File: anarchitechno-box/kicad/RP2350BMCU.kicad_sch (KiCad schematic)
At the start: 49 parts, among them J2 Conn_01x03_Socket, J4 C2988369, Q201 12mhz, SW1 C318884, U101 <value>, U201 TLV74311PDBVR, U21 C85364, U67 LP5907MFX-3.3

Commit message: Large intermediate schematic push. Remaining todos are on frontpage.
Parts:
- renumbered C3 to C10, C56 to C11, C28 to C12, C57 to C13, C58 to C14, C2 to C15, C4 to C16, C139 to C17, C5 to C18, C60 to C19, C26 to C20, C62 to C21, C33 to C22, C61 to C23, C150 to C24, C14 to C25, C16 to C26, C63 to C27, C65 to C28, C66 to C29, C51 to C3, C52 to C4, C53 to C5, C59 to C6, C54 to C7, C55 to C8, C140 to C9, J4 to J1, L3 to L1, Q201 to Q1, R204 to R1, R17 to R10, R18 to R11, R205 to R2, R33 to R3, R34 to R4, R35 to R5, R25 to R6, R202 to R7, R28 to R8, R26 to R9, U$2 to U$1, U101 to U4, U67 to U5, U201 to U6, U21 to U7, U3 to U8
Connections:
- net LED_STRING: now also U8.78 (GPIO1); no longer U8.79 (GPIO2)
- net PWM2_A: now reaches U8.1 (GPIO4)
- net PWM6_A: now reaches U8.11 (GPIO12)
- net PWM7_A: now reaches U8.13 (GPIO14)
- net ETH_MOSI: now reaches U8.19 (GPIO19)
- net ETH_MISO: now reaches U8.20 (GPIO20)
- net ETH_CS: now reaches U8.21 (GPIO21)
- net ETH_SCK: now reaches U8.22 (GPIO22)
- net DRV_SCK: now reaches U8.28 (GPIO27)
- net PWM3_A: now reaches U8.3 (GPIO6)
- net DRV_MOSI: now reaches U8.36 (GPIO28)
- net DRV_MISO: now reaches U8.38 (GPIO30)
- net DRV_nFAULT: now reaches U8.39 (GPIO31)
- net I2C0_SCL: now reaches U8.40 (GPIO32)
- net I2C0_SDA: now reaches U8.42 (GPIO33)
- net UART0_TX: now reaches U8.43 (GPIO34)
- net UART0_RX: now reaches U8.44 (GPIO35)
- net UART1_TX: now reaches U8.45 (GPIO36)
- net UART1_RX: now reaches U8.46 (GPIO37)
- net I2C1_SCL: now reaches U8.47 (GPIO38)
- net I2C1_SDA: now reaches U8.48 (GPIO39)
- net PWM8_A: now reaches U8.49 (GPIO40_ADC0)
- net DRV_CS1: now reaches U8.52 (GPIO41_ADC1)
- net PWM9_A: now reaches U8.53 (GPIO42_ADC2)
- net DRV_CS2: now reaches U8.54 (GPIO43_ADC3)
- net PWM10_A: now reaches U8.55 (GPIO44_ADC4)
- net DRV_CS3: now reaches U8.56 (GPIO45_ADC5)
- net PWM11_A: now reaches U8.57 (GPIO46_ADC6)
- net DRV_CS4: now reaches U8.58 (GPIO47_ADC7)
- net PWM4_A: now reaches U8.6 (GPIO8)
- net PWM0_A: now reaches U8.77 (GPIO0)
- net PWM5_A: now reaches U8.8 (GPIO10)
- new net PMW1_A: U8.79 (GPIO2)
- no-connect marks 35 -> 10
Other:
- moved on the sheet: C10, C11, C12, C13, C14, C15, C16, C17, C18, C19, C20, C21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

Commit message: meer Stijn in de Trein
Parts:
- added D16: SS34, Diode_SMD:D_SMA, symbol Diode:SS34
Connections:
- net +5V: now also D16.1 (K); no longer J1.A4B9 (VBUS), J1.A9B4 (VBUS)
- new net BREAKOUT_5V: D16.2 (A), J1.A4B9 (VBUS), J1.A9B4 (VBUS)
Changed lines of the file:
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@@
 	(wire
 		(pts
-			(xy 187.96 240.03) (xy 207.01 240.03)
+			(xy 187.96 240.03) (xy 193.04 240.03)
 		)
 		(stroke
@@
 	)
 	(label "BREAKOUT_5V"
-		(at 189.23 240.03 0)
+		(at 193.04 240.03 0)
+		(effects
+			(font
+				(size 1.27 1.27)
+			)
+			(justify left bottom)
+		)
+	)
+	(label "BREAKOUT_5V"
+		(at 209.55 214.63 0)
 		(effects
 			(font
@@
 	)
 	(symbol
+		(lib_id "Diode:SS34")
+		(at 205.74 214.63 0)
+		(unit 1)
+		(exclude_from_sim no)
+		(in_bom yes)
+		(on_board yes)
+		(dnp no)
+		(fields_autoplaced yes)
+		(property "Reference" "D16"
+			(at 205.4225 208.28 0)
+			(effects
+				(font
+					(size 1.27 1.27)
+				)
+			)
+		)
+		(property "Value" "SS34"
+			(at 205.4225 210.82 0)
+			(effects
+				(font
+					(size 1.27 1.27)
+				)
+			)
+		)
+		(property "Footprint" "Diode_SMD:D_SMA"
+			(at 205.74 219.075 0)
+			(effects
+				(font
+					(size 1.27 1.27)
+				)
+				(hide yes)
+			)
+		)
+		(property "Datasheet" "https://www.vishay.com/docs/88751/ss32.pdf"
+			(at 205.74 214.63 0)
+			(effects
+				(font
+					(size 1.27 1.27)
+				)
+				(hide yes)
+			)
+		)
+		(property "Description" "40V 3A Schottky Diode, SMA"
+			(at 205.74 214.63 0)
+			(effects
+				(font
+					(size 1.27 1.27)
+				)
+				(hide yes)
+			)
+		)
+		(pin "2"
+		)
+		(pin "1"
+		)
+		(instances
+			(project ""
+				(path "/8c734c41-38ed-40fc-83bd-134786dcfb35/d16ac510-e9e9-486e-8ddb-b850ff4462be"
+					(reference "D16")
+					(unit 1)
+				)
+			)
+		)
+	)
+	(symbol
 		(lib_id "power:+3.3V")
 		(at 90.17 246.38 270)
@@
 	(symbol
 		(lib_id "power:+5V")
-		(at 207.01 240.03 0)
+		(at 201.93 214.63 0)
 		(unit 1)
 		(exclude_from_sim no)
@@
 		(fields_autoplaced yes)
 		(property "Reference" "#PWR044"
-			(at 207.01 243.84 0)
+			(at 201.93 218.44 0)
 			(effects
 				(font
@@
 		)
 		(property "Value" "+5V"
-			(at 207.01 234.95 0)
+			(at 201.93 209.55 0)
 			(effects
 				(font
@@
 		)
 		(property "Footprint" ""
-			(at 207.01 240.03 0)
+			(at 201.93 214.63 0)
 			(effects
 				(font
@@
 		)
 		(property "Datasheet" ""
-			(at 207.01 240.03 0)
+			(at 201.93 214.63 0)
 			(effects
 				(font
@@
 		)
 		(property "Description" "Power symbol creates a global label with name \"+5V\""
-			(at 207.01 240.03 0)
+			(at 201.93 214.63 0)
 			(effects
 				(font

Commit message: trein trein trein
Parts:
- added C27: 100nF, Capacitor_SMD:C_0402_1005Metric, symbol TINRS - Wobbler (pico)sch-eagle-import:C-0402
- added C93: 10uF, Capacitor_SMD:C_0603_1608Metric, symbol Device:C
- added J8: Conn_01x04, Connector_PinHeader_2.54mm:PinHeader_1x04_P2.54mm_Vertical, symbol Connector_Generic:Conn_01x04
- added R47, R48: 2k, Resistor_SMD:R_0402_1005Metric, symbol TINRS - Wobbler (pico)sch-eagle-import:R-0402
- added SW2: RotaryEncoder_Switch_MP, Rotary_Encoder:RotaryEncoder_Alps_EC11E-Switch_Vertical_H20mm_CircularMountingHoles, symbol Device:RotaryEncoder_Switch_MP
- renumbered C27 to C92
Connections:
- net +3V3: now also C27.2, C93.1, J8.2 (Pin_2), R47.1, R48.1
- net GND: now also C27.1, C93.2, J8.1 (Pin_1), SW2.C, SW2.MP, SW2.S2
- net DISP_SDA: now reaches U8.16 (GPIO16)
- net DISP_SDA: now also J8.4 (Pin_4), R47.2
- net DISP_SCL: now reaches U8.17 (GPIO17)
- net DISP_SCL: now also J8.3 (Pin_3), R48.2
- new net ENC_A: SW2.A
- new net ENC_B: SW2.B
- new net ENC_S: SW2.S1
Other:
- moved on the sheet: C92

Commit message: choo choooooo
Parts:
- added J10: Conn_01x04, Connector_PinHeader_2.54mm:PinHeader_1x04_P2.54mm_Vertical, symbol Connector_Generic:Conn_01x04
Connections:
- net +3V3: now also J10.2 (Pin_2)
- net DISP_SCL: now also J10.4 (Pin_4)
- net DISP_SDA: now also J10.3 (Pin_3)
- net ENC_A: now also U8.18 (GPIO18)
- net ENC_B: now also U8.27 (GPIO26)
- net ENC_S: now also U8.14 (GPIO15)
- net GND: now also J10.1 (Pin_1)
- net I2C0_SCL: no longer names the net of U8.40 (GPIO32)
- net I2C0_SDA: no longer names the net of U8.42 (GPIO33)
- net I2C1_SCL: no longer names the net of U8.47 (GPIO38)
- net I2C1_SDA: no longer names the net of U8.48 (GPIO39)

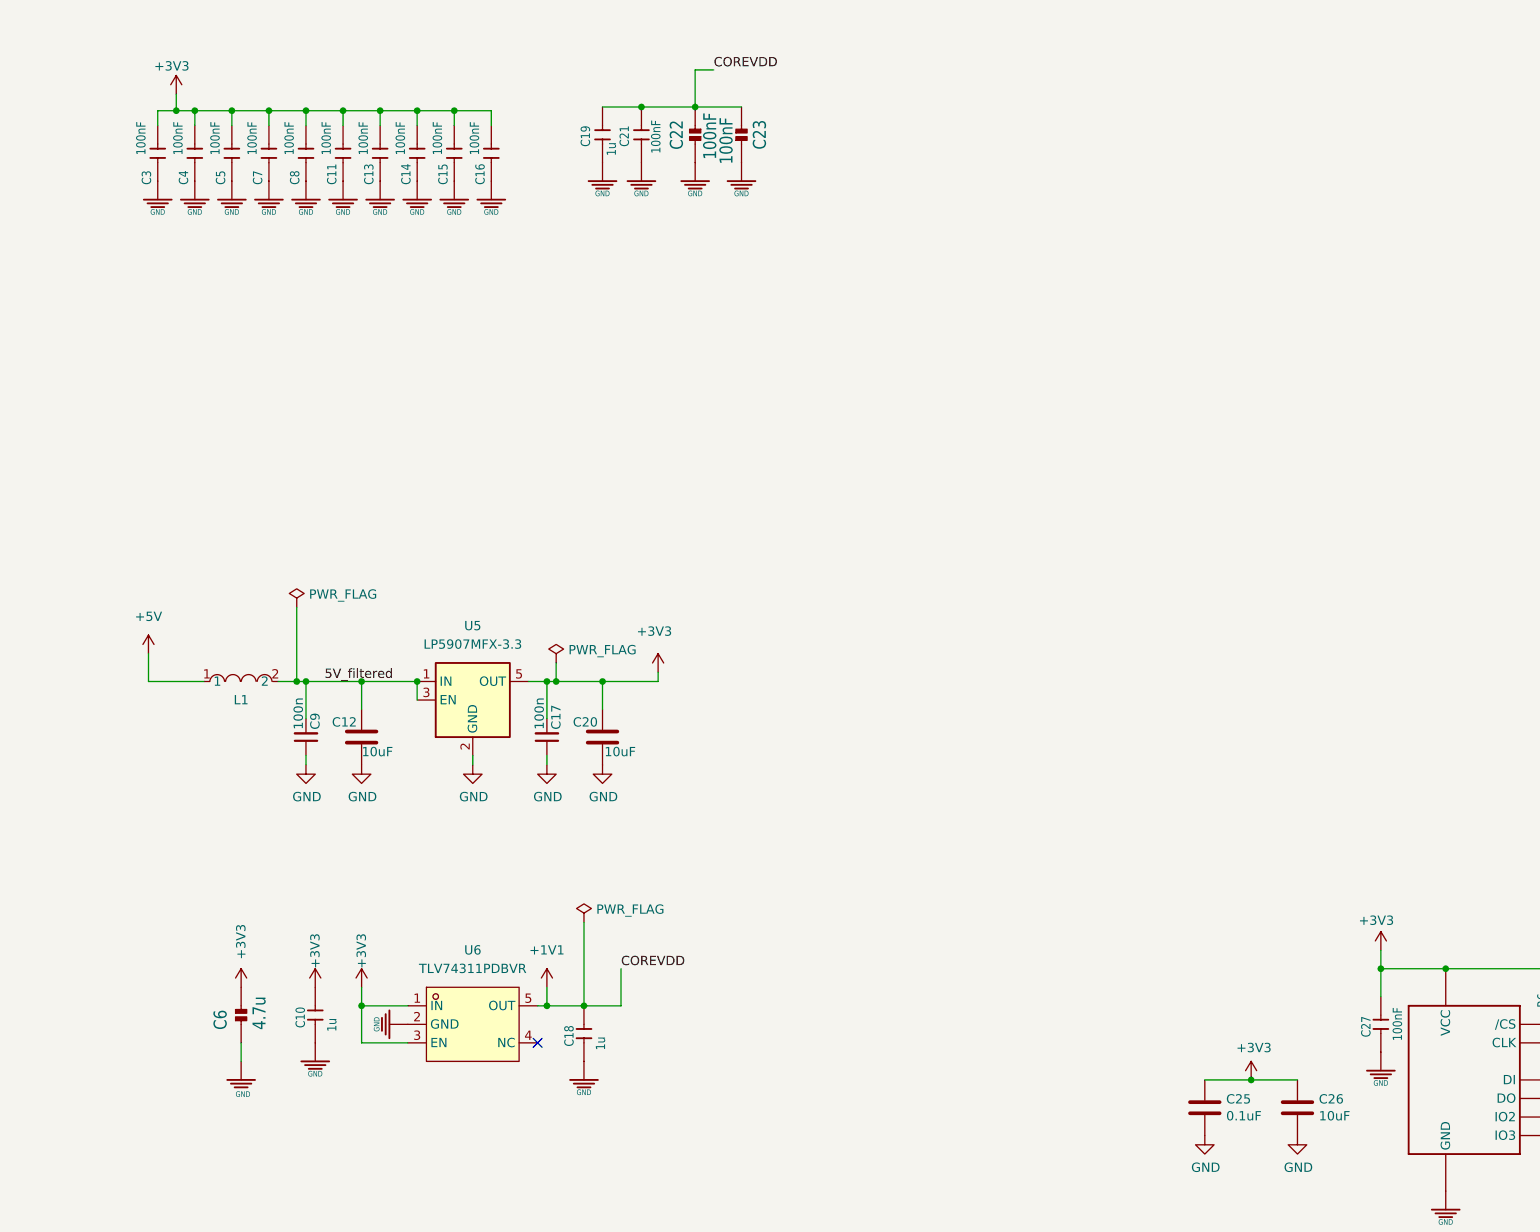
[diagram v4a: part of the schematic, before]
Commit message: 3.3V 1A regulator on high & low side
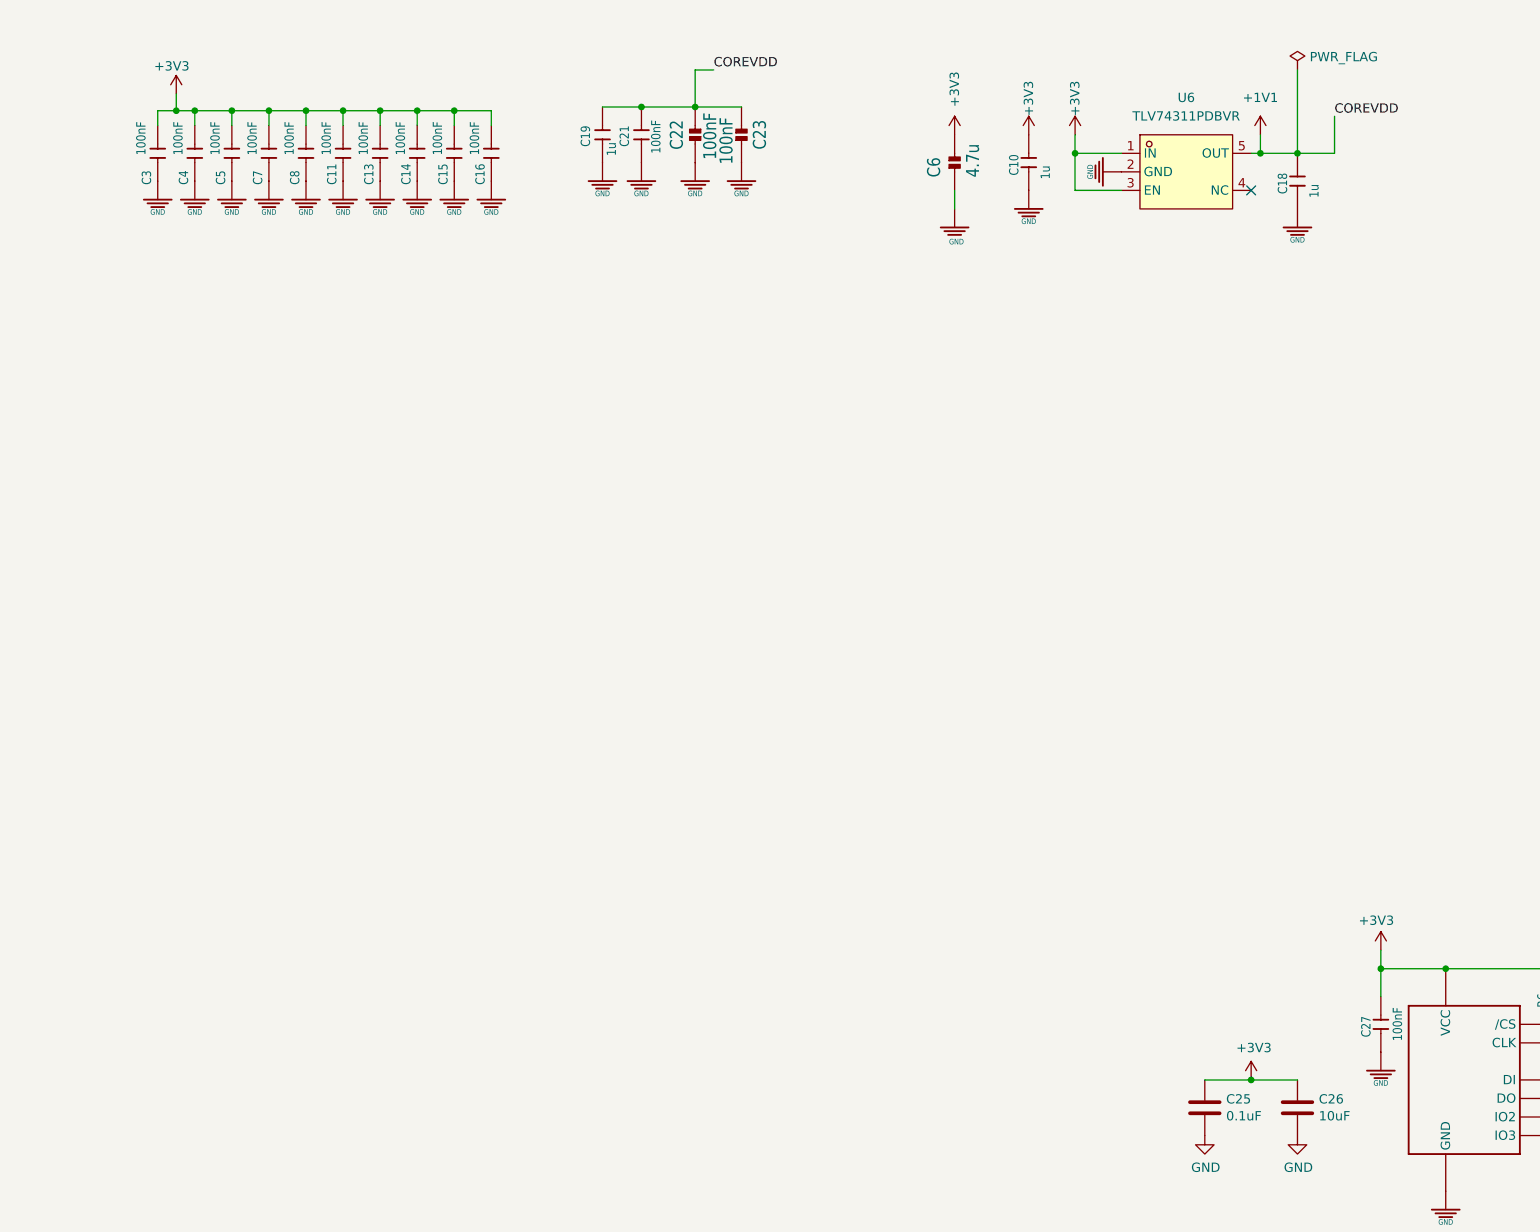
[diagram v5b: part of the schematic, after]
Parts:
- removed C12, C20: 10uF, Capacitor_SMD:C_0603_1608Metric, symbol Device:C
- removed C17, C9: 100n, Capacitor_SMD:C_0402_1005Metric, symbol Device:C_Small
- removed L1: BLM18PG121SN1D_C14709, BigFishImports:L0603, symbol BigFishImports:BLM18PG121SN1D_C14709
- removed U5: LP5907MFX-3.3, Package_TO_SOT_SMD:SOT-23-5, symbol Regulator_Linear:LP5907MFX-3.3
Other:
- moved on the sheet: C10, C18, C6, U6

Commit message: Re-added 1.1V regulator. Removed 3.3VDDA for Ethernet. Increased clearances on layout a bit..
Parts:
- U6: footprint jlcpcb3:SOT-23-5_L3.0-W1.7-P0.95-LS2.8-BL -> Package_TO_SOT_SMD:SOT-23-5
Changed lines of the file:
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@@
 			)
 		)
-		(property "Footprint" "jlcpcb3:SOT-23-5_L3.0-W1.7-P0.95-LS2.8-BL"
+		(property "Footprint" "Package_TO_SOT_SMD:SOT-23-5"
 			(at 187.96 46.99 0)
 			(effects
